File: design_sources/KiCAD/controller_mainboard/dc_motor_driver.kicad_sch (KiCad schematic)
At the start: 34 parts, among them Q1 IRF3205, Q2 IRF3205, Q3 IRF3205, Q4 IRF3205, U3 HIP4082IBZT, U4 INA180A1IDBVR

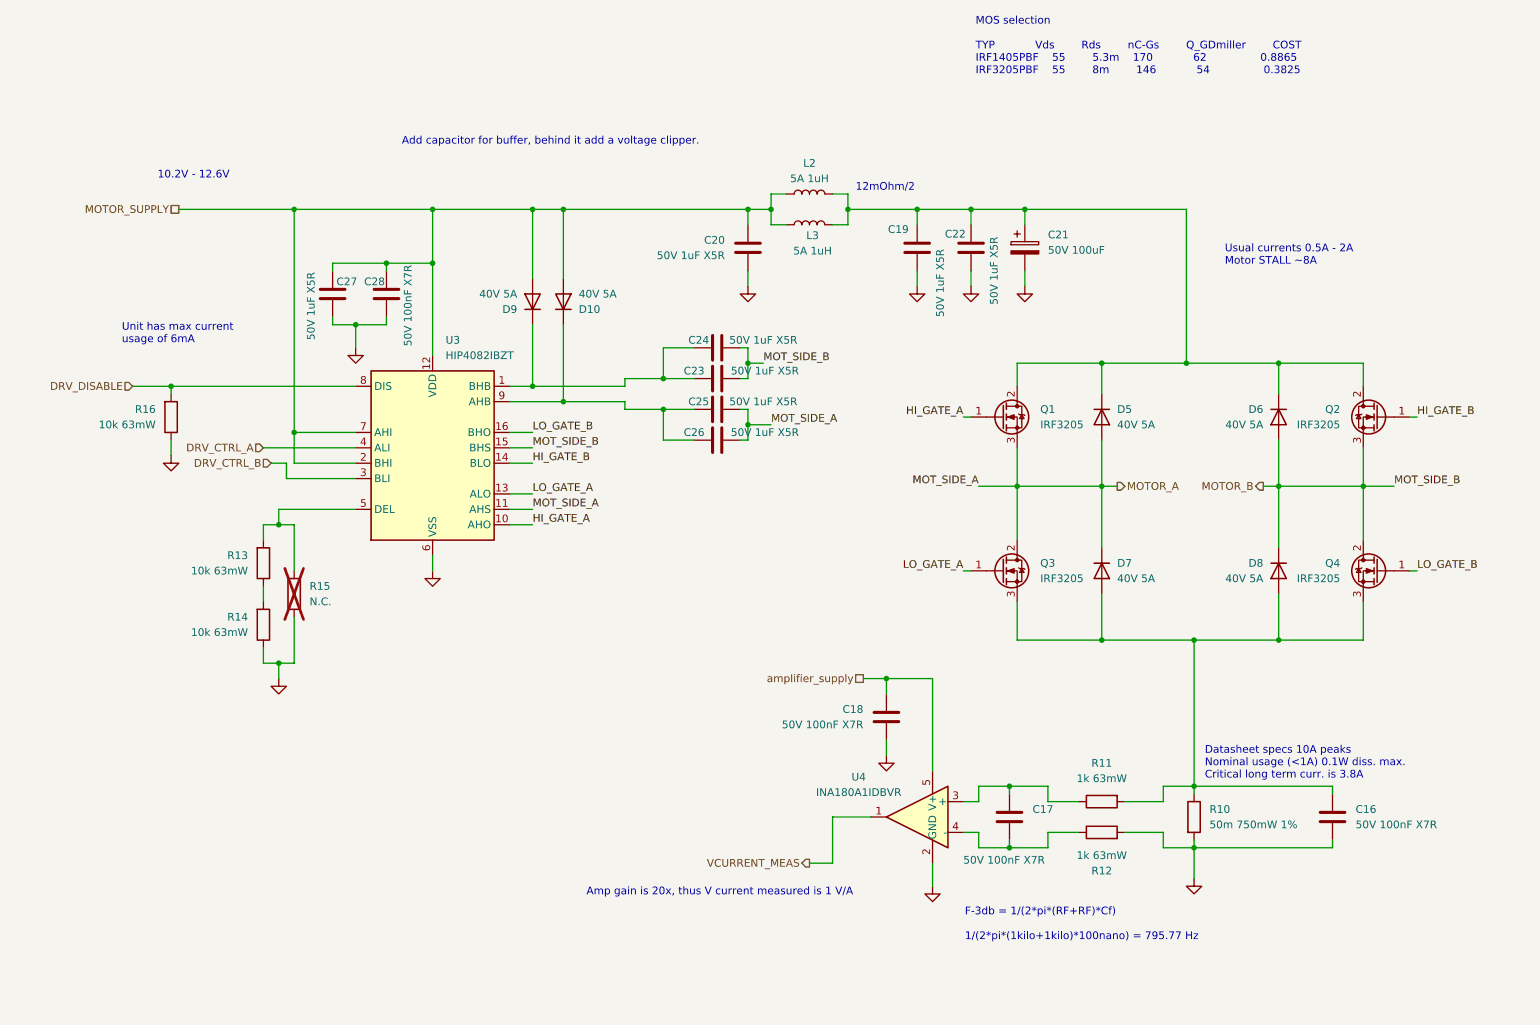
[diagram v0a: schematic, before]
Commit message: Populated the schematic more, added buck.
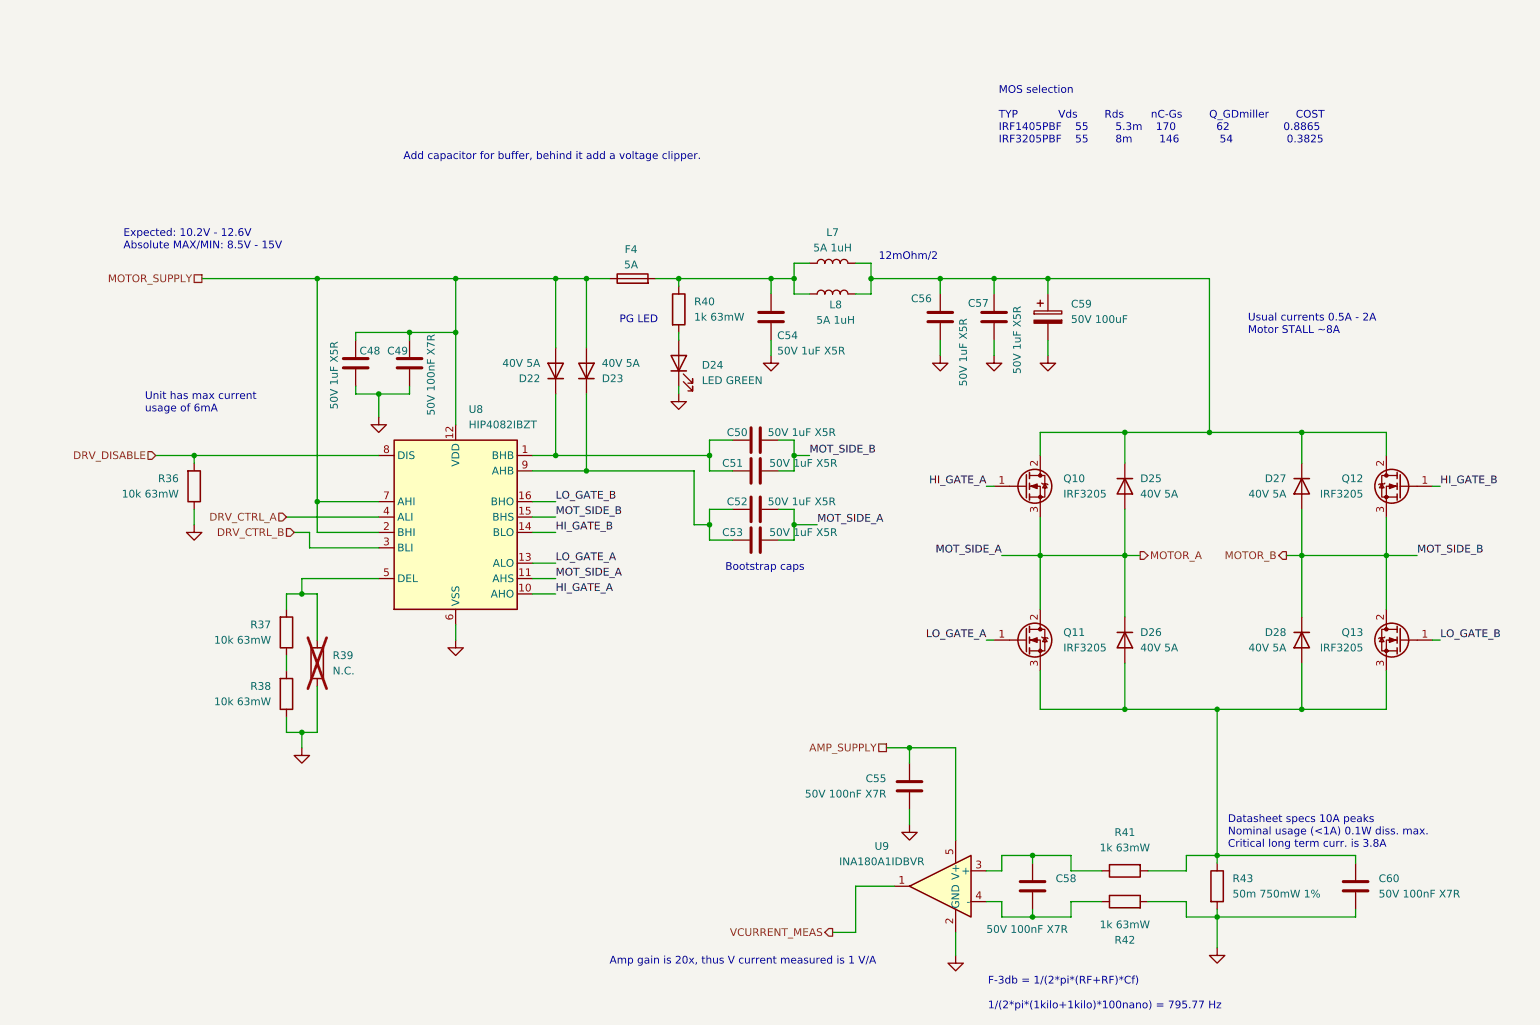
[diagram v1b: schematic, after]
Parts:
- added D24: LED GREEN, LED_SMD:LED_0805_2012Metric, symbol Device:LED
- added F4: 5A, Custom_feetprint:BLX-A fuse holder, symbol Device:Fuse
- added R40: 1k 63mW, Resistor_SMD:R_0402_1005Metric, symbol Device:R
- Q10: renamed from Q1; footprint Package_TO_SOT_THT:TO-220-3_Vertical -> Package_TO_SOT_THT:TO-220F-3_Horizontal_TabDown
- Q11: renamed from Q3; footprint Package_TO_SOT_THT:TO-220-3_Vertical -> Package_TO_SOT_THT:TO-220F-3_Horizontal_TabDown
- Q12: renamed from Q2; footprint Package_TO_SOT_THT:TO-220-3_Vertical -> Package_TO_SOT_THT:TO-220F-3_Horizontal_TabDown
- Q13: renamed from Q4; footprint Package_TO_SOT_THT:TO-220-3_Vertical -> Package_TO_SOT_THT:TO-220F-3_Horizontal_TabDown
- renumbered C27 to C48, C28 to C49, C24 to C50, C23 to C51, C25 to C52, C26 to C53, C20 to C54, C18 to C55, C19 to C56, C22 to C57, C17 to C58, C21 to C59, C16 to C60, D9 to D22, D10 to D23, D5 to D25, D7 to D26, D6 to D27, D8 to D28, L2 to L7, L3 to L8, R16 to R36, R13 to R37, R14 to R38, R15 to R39, R11 to R41, R12 to R42, R10 to R43, U3 to U8, U4 to U9
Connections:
- net GND: now also D24.1 (K)
- net MOTOR_SUPPLY: now also F4.1; no longer C54.1, L7.1, L8.2
- net amplifier_supply renamed AMP_SUPPLY
- new net: C54.1, F4.2, L7.1, L8.2, R40.1
- new net: D24.2 (A), R40.2
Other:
- note added: "Bootstrap caps"
- note added: "Expected: 10.2V - 12.6V Absolute MAX/MIN: 8.5V - 15V"
- note added: "PG LED"
- note removed: "10.2V - 12.6V"
- moved on the sheet: C48, C49, C50, C51, C52, C53, C54, C55, C56, C57, C58, C59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

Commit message: Continued development on the schematic. Pins wired. TODO validate.
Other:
- company: Kestech -> Mete Han Keskin
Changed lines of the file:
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@@
 		(date "2025-03-01")
 		(rev "V1.0")
-		(company "Kestech")
-		(comment 1 "MIT License. Copyright (c) 2025 Kestech Fontys")
+		(company "Mete Han Keskin")
+		(comment 1 "MIT License. Copyright (c) 2025 kestech.net")
 	)
 	(text "Usual currents 0.5A - 2A\nMotor STALL ~8A"

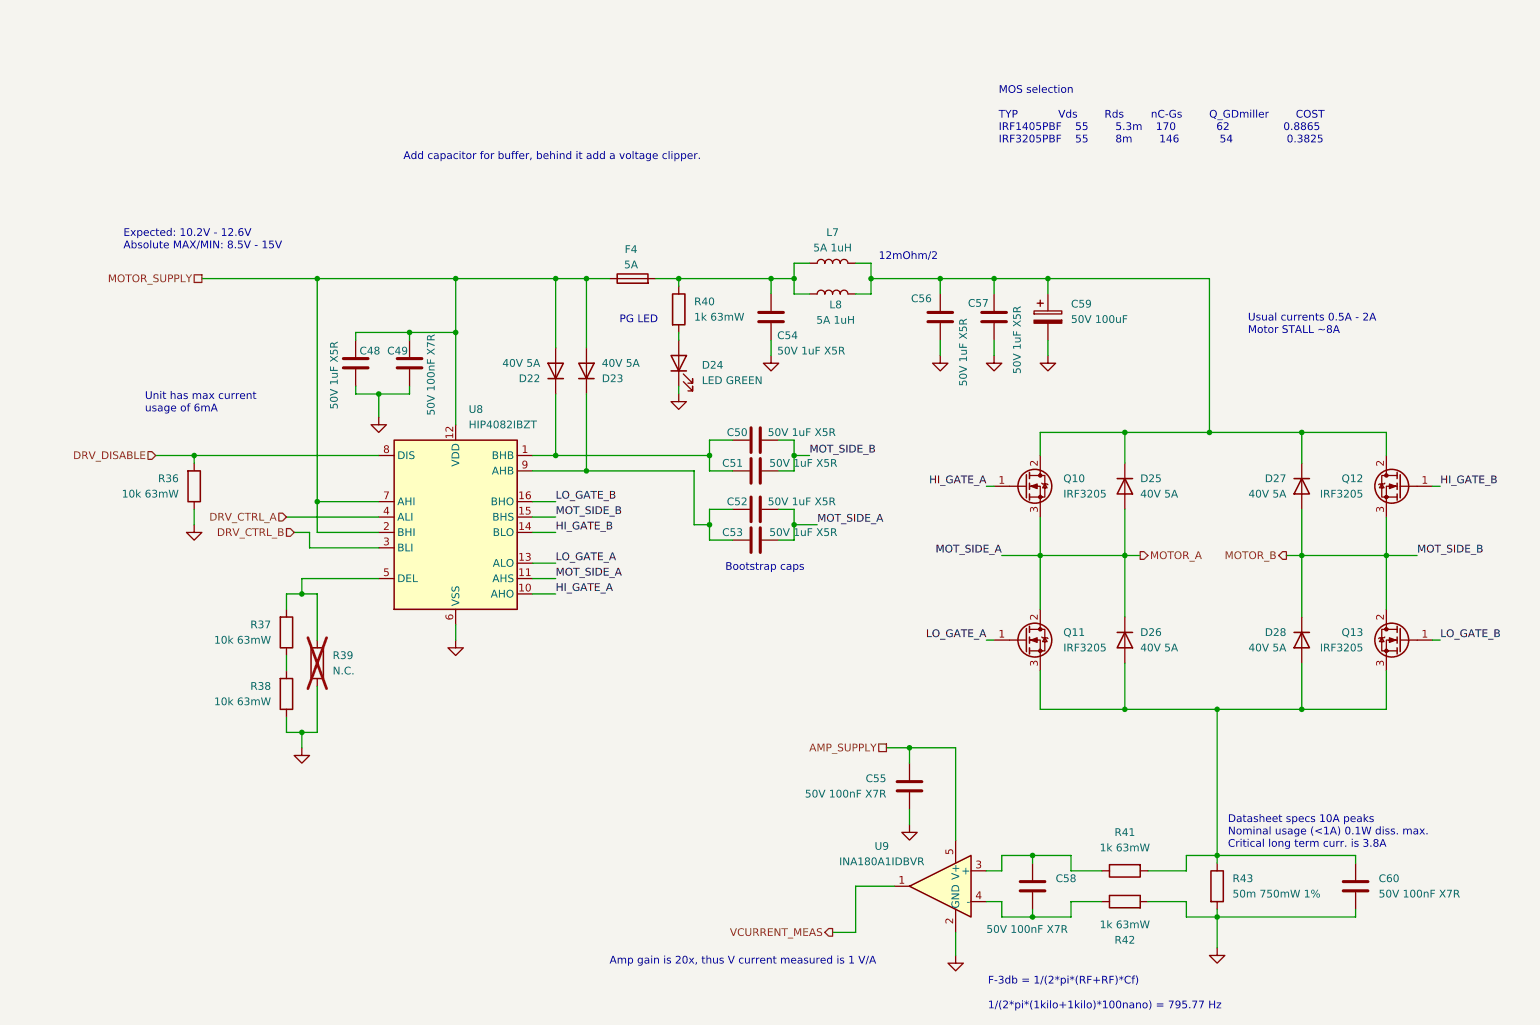
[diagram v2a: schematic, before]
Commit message: Added ESD protection ic, added footprints to all IC and loaded into pcbnew to size up the pcb size.
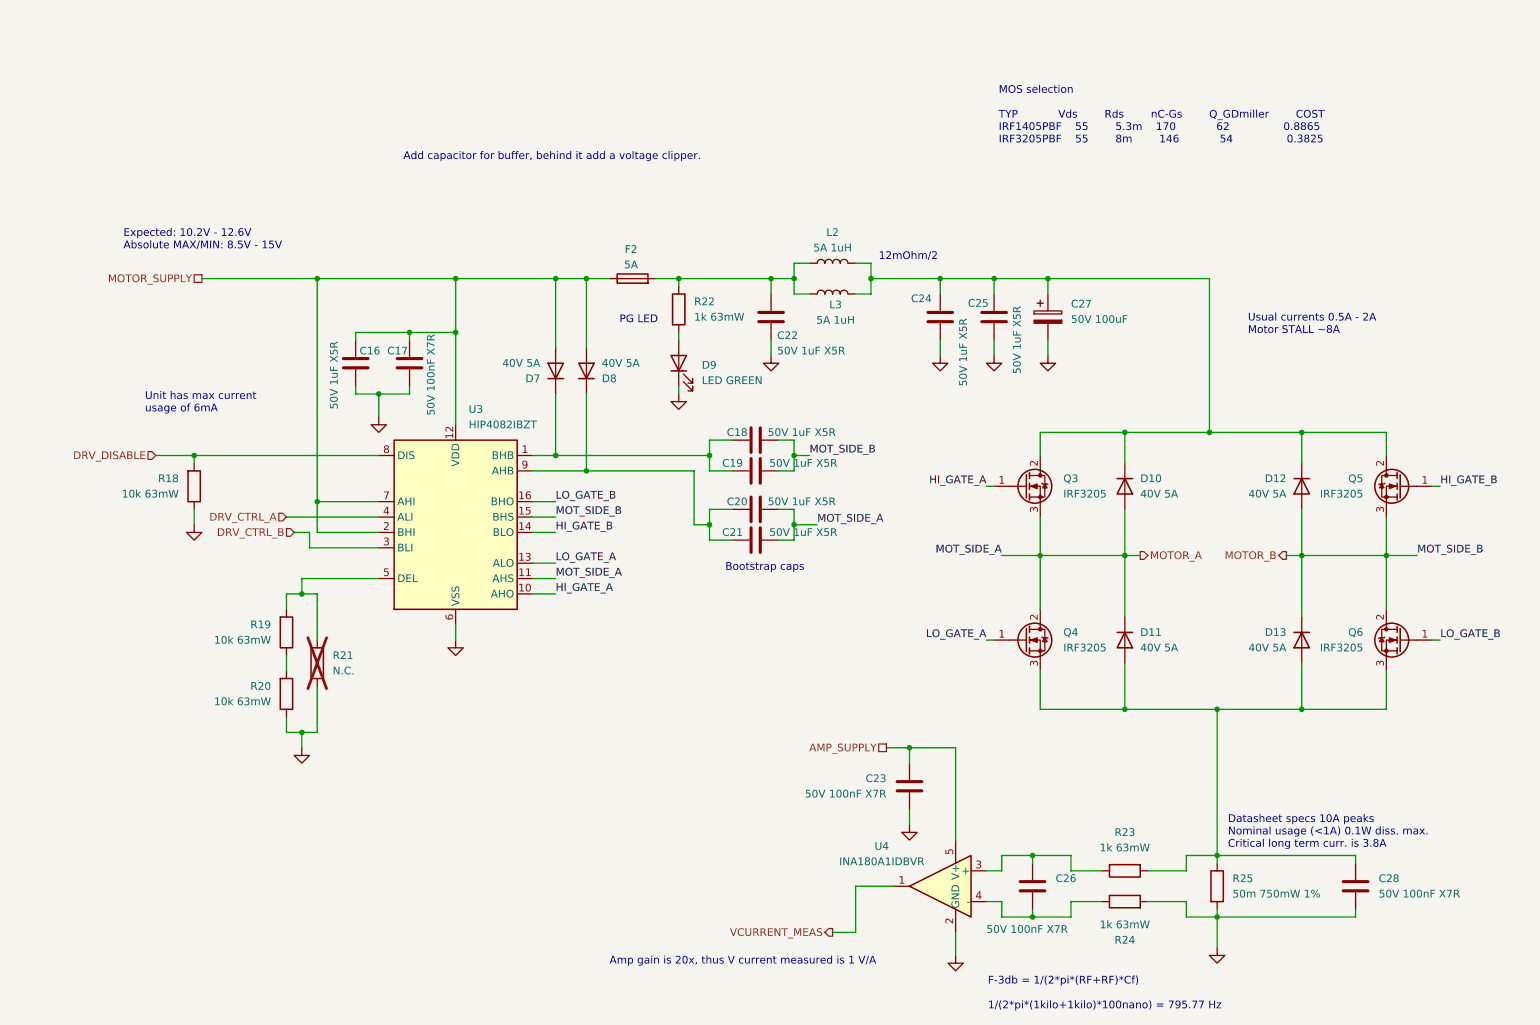
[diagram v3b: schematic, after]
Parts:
- L2: renamed from L7; footprint (none) -> Inductor_SMD:L_APV_ANR5040
- L3: renamed from L8; footprint (none) -> Inductor_SMD:L_APV_ANR5040
- renumbered C48 to C16, C49 to C17, C50 to C18, C51 to C19, C52 to C20, C53 to C21, C54 to C22, C55 to C23, C56 to C24, C57 to C25, C58 to C26, C59 to C27, C60 to C28, D25 to D10, D26 to D11, D27 to D12, D28 to D13, D22 to D7, D23 to D8, D24 to D9, F4 to F2, Q10 to Q3, Q11 to Q4, Q12 to Q5, Q13 to Q6, R36 to R18, R37 to R19, R38 to R20, R39 to R21, R40 to R22, R41 to R23, R42 to R24, R43 to R25, U8 to U3, U9 to U4

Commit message: Read through schematic to bugfix.
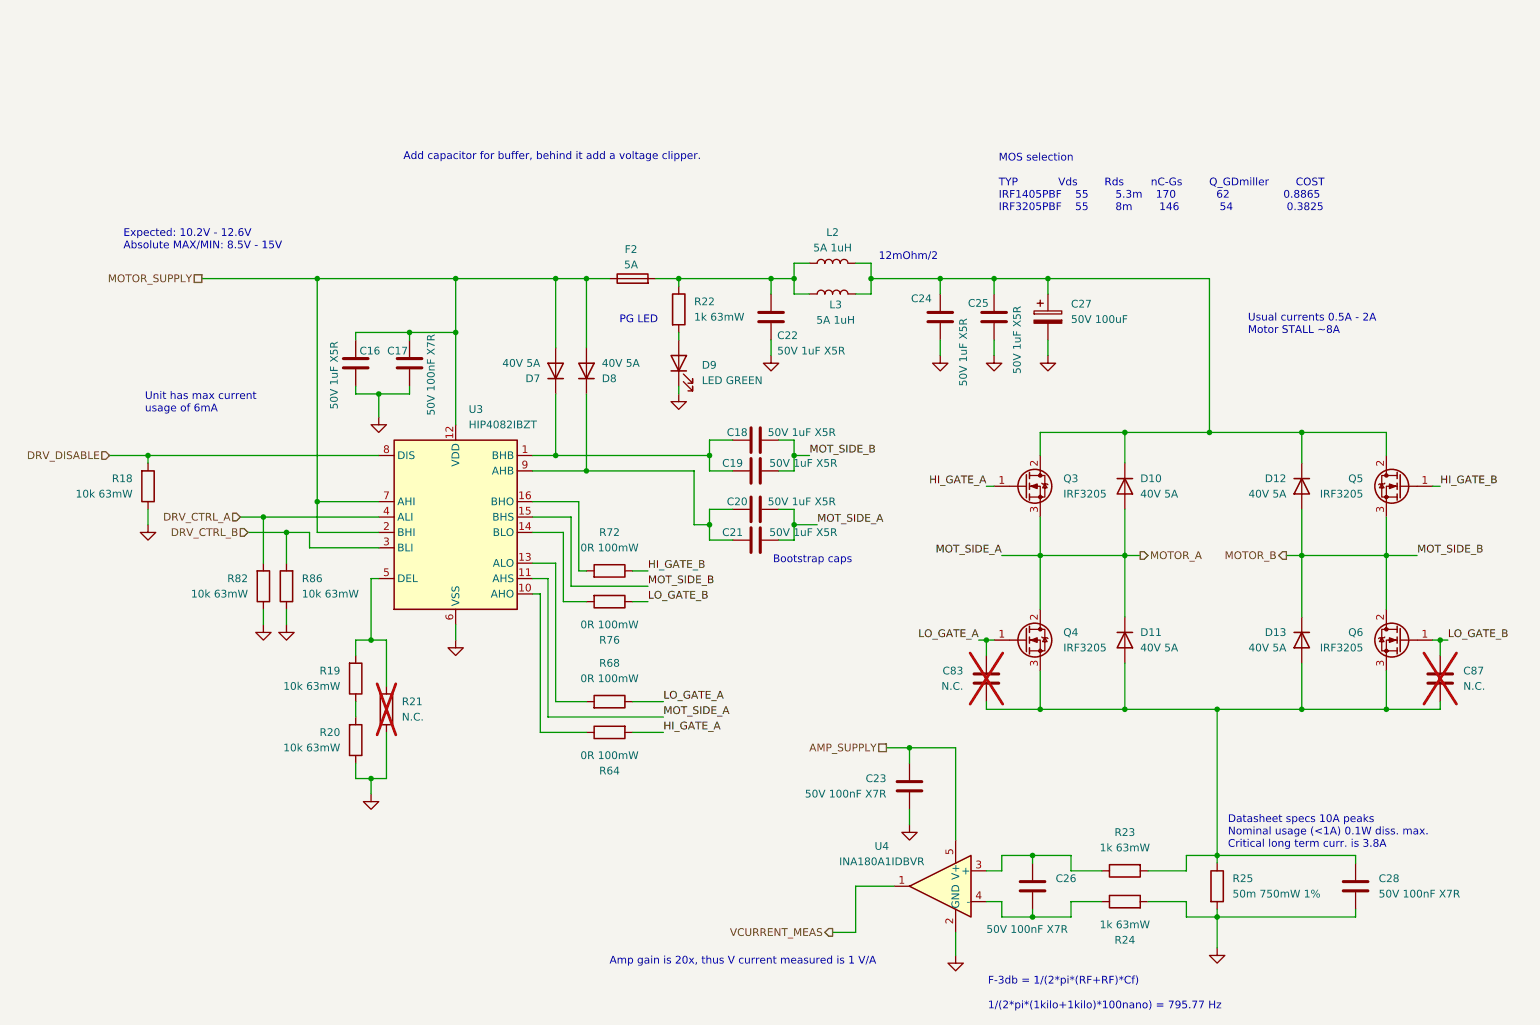
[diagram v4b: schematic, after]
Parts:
- added C83, C87: N.C., Capacitor_SMD:C_0603_1608Metric, symbol Device:C
- added R64, R68, R72, R76: 0R 100mW, Resistor_SMD:R_0603_1608Metric, symbol Device:R
- added R82, R86: 10k 63mW, Resistor_SMD:R_0402_1005Metric, symbol Device:R
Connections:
- net DRV_CTRL_A: now also R82.2
- net DRV_CTRL_B : now also R86.2
- net GND: now also R82.1, R86.1
- net HI_GATE_A: now also R64.2; no longer U3.10 (AHO)
- net HI_GATE_B: now also R72.1; no longer U3.14 (BLO)
- net LO_GATE_A: now also C83.2, R68.1; no longer U3.13 (ALO)
- net LO_GATE_B: now also C87.2, R76.1; no longer U3.16 (BHO)
- net at C28.2, D11.2 (A), D13.2 (A)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: now also C83.1, C87.1
- new net: R72.2, U3.16 (BHO)
- new net: R68.2, U3.13 (ALO)
- new net: R64.1, U3.10 (AHO)
- new net: R76.2, U3.14 (BLO)
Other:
- moved on the sheet: R18, R19, R20, R21

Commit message: started initial pcb layout
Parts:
- Q3, Q4, Q5, Q6: footprint Package_TO_SOT_THT:TO-220F-3_Horizontal_TabDown -> Package_TO_SOT_THT:TO-220-3_Horizontal_TabDown
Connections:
- net MOTOR_SUPPLY: no longer C16.1, C17.2, D7.2 (A), D8.2 (A), U3.12 (VDD), U3.2 (BHI), U3.7 (AHI)
- net at C22.1, F2.2, L2.1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: now also C16.1, C17.2, D7.2 (A), D8.2 (A), U3.12 (VDD), U3.2 (BHI), U3.7 (AHI)
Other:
- moved on the sheet: F2
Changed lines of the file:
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@@
 	(text "Expected: 10.2V - 12.6V\nAbsolute MAX/MIN: 8.5V - 15V"
 		(exclude_from_sim no)
-		(at 30.226 33.782 0)
+		(at 32.004 29.464 0)
 		(effects
 			(font
@@
 	(wire
 		(pts
+			(xy 55.88 41.91) (xy 62.23 41.91)
+		)
+		(stroke
+			(width 0)
+			(type default)
+		)
+	)
+	(wire
+		(pts
 			(xy 77.47 59.69) (xy 77.47 60.96)
 		)
@@
 	(wire
 		(pts
-			(xy 106.68 41.91) (xy 110.49 41.91)
+			(xy 106.68 41.91) (xy 121.92 41.91)
 		)
 		(stroke
@@
 	(wire
 		(pts
-			(xy 118.11 41.91) (xy 121.92 41.91)
-		)
-		(stroke
-			(width 0)
-			(type default)
-		)
-	)
-	(wire
-		(pts
 			(xy 104.14 92.71) (xy 104.14 81.28)
 		)
@@
 	(wire
 		(pts
-			(xy 43.18 41.91) (xy 62.23 41.91)
+			(xy 30.48 41.91) (xy 48.26 41.91)
 		)
 		(stroke
@@
 	(hierarchical_label "MOTOR_SUPPLY"
 		(shape passive)
-		(at 43.18 41.91 180)
+		(at 30.48 41.91 180)
 		(effects
 			(font
@@
 			)
 		)
-		(property "Footprint" "Package_TO_SOT_THT:TO-220F-3_Horizontal_TabDown"
+		(property "Footprint" "Package_TO_SOT_THT:TO-220-3_Horizontal_TabDown"
 			(at 184.15 78.105 0)
 			(effects
@@
 			)
 		)
-		(property "Footprint" "Package_TO_SOT_THT:TO-220F-3_Horizontal_TabDown"
+		(property "Footprint" "Package_TO_SOT_THT:TO-220-3_Horizontal_TabDown"
 			(at 236.22 78.105 0)
 			(effects
@@
 	(symbol
 		(lib_id "Device:Fuse")
-		(at 114.3 41.91 90)
+		(at 52.07 41.91 90)
 		(unit 1)
 		(exclude_from_sim no)
@@
 		(dnp no)
 		(property "Reference" "F2"
-			(at 114.046 37.084 90)
+			(at 51.816 37.084 90)
 			(effects
 				(font
@@
 		)
 		(property "Value" "5A"
-			(at 114.046 39.624 90)
+			(at 51.816 39.624 90)
 			(effects
 				(font
@@
 		)
 		(property "Footprint" "Custom_feetprint:BLX-A fuse holder"
-			(at 114.3 43.688 90)
+			(at 52.07 43.688 90)
 			(effects
 				(font
@@
 		)
 		(property "Datasheet" "~"
-			(at 114.3 41.91 0)
+			(at 52.07 41.91 0)
 			(effects
 				(font
@@
 		)
 		(property "Description" "Fuse"
-			(at 114.3 41.91 0)
+			(at 52.07 41.91 0)
 			(effects
 				(font
@@
 			)
 		)
-		(property "Footprint" "Package_TO_SOT_THT:TO-220F-3_Horizontal_TabDown"
+		(property "Footprint" "Package_TO_SOT_THT:TO-220-3_Horizontal_TabDown"
 			(at 236.22 103.505 0)
 			(effects
@@
 			)
 		)
-		(property "Footprint" "Package_TO_SOT_THT:TO-220F-3_Horizontal_TabDown"
+		(property "Footprint" "Package_TO_SOT_THT:TO-220-3_Horizontal_TabDown"
 			(at 184.15 103.505 0)
 			(effects
